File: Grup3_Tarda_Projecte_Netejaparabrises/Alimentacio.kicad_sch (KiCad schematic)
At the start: 8 parts, among them J1 Screw_Terminal_01x02, U1 LM1117MP-5.0

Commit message: canvis schematic 05-04-23
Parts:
- added D8: LED, symbol Device:LED
- added R6: 220, symbol Device:R
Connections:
- net +VCC: now also D8.2 (A)
- net GND: now also R6.2
- new net Vled: D8.1 (K), R6.1

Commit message: canvis schematic i README 07-04-2023
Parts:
- removed U1: LM1117MP-5.0, Package_TO_SOT_SMD:SOT-223-3_TabPin2, symbol Regulator_Linear:LM1117MP-5.0
- added IC1: L78S05CV, TO-220-STANDING, symbol L78S05CV:L78S05CV
- C2: value 1u -> 0.33u
- C4: value 1u -> 0.1u
- D2: value 15V -> 35V
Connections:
- net +VCC: now also IC1.3
- net GND: now also IC1.2
- net V_{in}: now also IC1.1
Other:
- moved on the sheet: C4
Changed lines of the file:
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@@
     (rev "v1.1.05042023")
   )
+  (junction (at 132.334 62.992) (diameter 0) (color 0 0 0 0)
+  )
   (junction (at 113.284 62.992) (diameter 0) (color 0 0 0 0)
   )
-  (junction (at 132.334 62.992) (diameter 0) (color 0 0 0 0)
-  )
   (junction (at 120.904 84.582) (diameter 0) (color 0 0 0 0)
   )
   (junction (at 132.334 84.582) (diameter 0) (color 0 0 0 0)
   )
+  (junction (at 157.988 62.992) (diameter 0) (color 0 0 0 0)
+  )
   (junction (at 178.054 62.992) (diameter 0) (color 0 0 0 0)
   )
@@
   (junction (at 147.574 84.582) (diameter 0) (color 0 0 0 0)
   )
-  (junction (at 157.988 62.992) (diameter 0) (color 0 0 0 0)
-  )
   (junction (at 157.988 84.582) (diameter 0) (color 0 0 0 0)
   )
@@
     (stroke (width 0) (type default))
   )
-  (wire (pts (xy 178.054 71.882) (xy 178.054 84.582))
-    (stroke (width 0) (type default))
-  )
-  (wire (pts (xy 178.054 62.992) (xy 178.054 64.262))
+  (wire (pts (xy 132.334 62.992) (xy 139.954 62.992))
+    (stroke (width 0) (type default))
+  )
+  (wire (pts (xy 178.054 72.136) (xy 178.054 84.582))
+    (stroke (width 0) (type default))
+  )
+  (wire (pts (xy 178.054 62.992) (xy 178.054 64.516))
     (stroke (width 0) (type default))
   )
@@
     (stroke (width 0) (type default))
   )
+  (wire (pts (xy 99.314 62.992) (xy 100.584 62.992))
+    (stroke (width 0) (type default))
+  )
+  (wire (pts (xy 178.054 62.992) (xy 181.864 62.992))
+    (stroke (width 0) (type default))
+  )
   (wire (pts (xy 155.194 62.992) (xy 157.988 62.992))
     (stroke (width 0) (type default))
   )
-  (wire (pts (xy 99.314 62.992) (xy 100.584 62.992))
-    (stroke (width 0) (type default))
-  )
-  (wire (pts (xy 178.054 62.992) (xy 181.864 62.992))
-    (stroke (width 0) (type default))
-  )
   (wire (pts (xy 120.904 62.992) (xy 120.904 64.262))
     (stroke (width 0) (type default))
@@
     (stroke (width 0) (type default))
   )
-  (wire (pts (xy 132.334 62.992) (xy 139.954 62.992))
-    (stroke (width 0) (type default))
-  )
   (wire (pts (xy 132.334 84.582) (xy 147.574 84.582))
     (stroke (width 0) (type default))
@@
     (stroke (width 0) (type default))
   )
-  (wire (pts (xy 167.894 69.342) (xy 167.894 84.582))
+  (wire (pts (xy 167.894 70.612) (xy 167.894 84.582))
     (stroke (width 0) (type default))
   )
@@
     (stroke (width 0) (type default))
   )
-  (wire (pts (xy 167.894 62.992) (xy 167.894 64.262))
+  (wire (pts (xy 167.894 62.992) (xy 167.894 65.532))
     (stroke (width 0) (type default))
   )
@@
     )
   )
-  (symbol (lib_id "Device:C_Polarized_Small_US") (at 167.894 66.802 0) (unit 1)
+  (symbol (lib_id "Device:C_Polarized_Small_US") (at 167.894 68.072 0) (unit 1)
     (in_bom yes) (on_board yes) (dnp no)
-    (property "Reference" "C4" (at 170.18 65.532 0)
-      (effects (font (size 1.27 1.27)) (justify left))
-    )
-    (property "Value" "1u" (at 170.18 68.072 0)
-      (effects (font (size 1.27 1.27)) (justify left))
-    )
-    (property "Footprint" "Capacitor_THT:C_Disc_D3.0mm_W1.6mm_P2.50mm" (at 167.894 66.802 0)
-      (effects (font (size 1.27 1.27)) hide)
-    )
-    (property "Datasheet" "~" (at 167.894 66.802 0)
+    (property "Reference" "C4" (at 170.18 66.802 0)
+      (effects (font (size 1.27 1.27)) (justify left))
+    )
+    (property "Value" "0.1u" (at 170.18 69.342 0)
+      (effects (font (size 1.27 1.27)) (justify left))
+    )
+    (property "Footprint" "Capacitor_THT:C_Disc_D3.0mm_W1.6mm_P2.50mm" (at 167.894 68.072 0)
+      (effects (font (size 1.27 1.27)) hide)
+    )
+    (property "Datasheet" "~" (at 167.894 68.072 0)
       (effects (font (size 1.27 1.27)) hide)
     )
@@
     )
   )
-  (symbol (lib_id "Regulator_Linear:LM1117MP-5.0") (at 147.574 62.992 0) (unit 1)
+  (symbol (lib_id "L78S05CV:L78S05CV") (at 147.574 62.992 0) (unit 1)
     (in_bom yes) (on_board yes) (dnp no) (fields_autoplaced)
-    (property "Reference" "U1" (at 147.574 56.896 0)
-      (effects (font (size 1.27 1.27)))
-    )
-    (property "Value" "LM1117MP-5.0" (at 147.574 59.436 0)
-      (effects (font (size 1.27 1.27)))
-    )
-    (property "Footprint" "Package_TO_SOT_SMD:SOT-223-3_TabPin2" (at 147.574 62.992 0)
-      (effects (font (size 1.27 1.27)) hide)
-    )
-    (property "Datasheet" "http://www.ti.com/lit/ds/symlink/lm1117.pdf" (at 147.574 62.992 0)
-      (effects (font (size 1.27 1.27)) hide)
+    (property "Reference" "IC1" (at 147.574 55.88 0)
+      (effects (font (size 1.27 1.27)))
+    )
+    (property "Value" "L78S05CV" (at 147.574 58.42 0)
+      (effects (font (size 1.27 1.27)))
+    )
+    (property "Footprint" "TO-220-STANDING" (at 147.574 62.992 0)
+      (effects (font (size 1.27 1.27)) (justify bottom) hide)
+    )
+    (property "Datasheet" "" (at 147.574 62.992 0)
+      (effects (font (size 1.27 1.27)) hide)
+    )
+    (property "VOUT" "5.0 V" (at 147.574 62.992 0)
+      (effects (font (size 1.27 1.27)) (justify bottom) hide)
+    )
+    (property "MANUFACTURER" "St Microelectronics" (at 147.574 62.992 0)
+      (effects (font (size 1.27 1.27)) (justify bottom) hide)
+    )
+    (property "CURRENT" "2.0 A" (at 147.574 62.992 0)
+      (effects (font (size 1.27 1.27)) (justify bottom) hide)
+    )
+    (property "TME" "L78S05CV" (at 147.574 62.992 0)
+      (effects (font (size 1.27 1.27)) (justify bottom) hide)
+    )
+    (property "PACKAGE" "TO-220" (at 147.574 62.992 0)
+      (effects (font (size 1.27 1.27)) (justify bottom) hide)
+    )
+    (property "VIN-MAX" "35.0 V" (at 147.574 62.992 0)
+      (effects (font (size 1.27 1.27)) (justify bottom) hide)
+    )
+    (property "VIN-MIN" "8.0 V" (at 147.574 62.992 0)
+      (effects (font (size 1.27 1.27)) (justify bottom) hide)
     )
     (pin "1")
@@
       (project "Grup3_Tarda_Projecte_Netejaparabrises"
         (path "/7ae78f34-680b-4fd9-8391-ce3e1c73c4b5/de573664-441d-44bf-8893-2d2e822d4a99"
-          (reference "U1") (unit 1)
+          (reference "IC1") (unit 1)
         )
       )
@@
       (effects (font (size 1.27 1.27)) (justify left))
     )
-    (property "Value" "1u" (at 134.366 69.596 0)
+    (property "Value" "0.33u" (at 134.366 69.596 0)
       (effects (font (size 1.27 1.27)) (justify left))
     )
@@
     )
   )
-  (symbol (lib_id "Device:C") (at 178.054 68.072 0) (unit 1)
+  (symbol (lib_id "Device:C") (at 178.054 68.326 0) (unit 1)
     (in_bom yes) (on_board yes) (dnp no)
-    (property "Reference" "C5" (at 181.102 66.802 0)
-      (effects (font (size 1.27 1.27)) (justify left))
-    )
-    (property "Value" "100n" (at 181.102 69.342 0)
-      (effects (font (size 1.27 1.27)) (justify left))
-    )
-    (property "Footprint" "Capacitor_SMD:C_0805_2012Metric" (at 179.0192 71.882 0)
-      (effects (font (size 1.27 1.27)) hide)
-    )
-    (property "Datasheet" "~" (at 178.054 68.072 0)
+    (property "Reference" "C5" (at 181.102 67.056 0)
+      (effects (font (size 1.27 1.27)) (justify left))
+    )
+    (property "Value" "100n" (at 181.102 69.596 0)
+      (effects (font (size 1.27 1.27)) (justify left))
+    )
+    (property "Footprint" "Capacitor_SMD:C_0805_2012Metric" (at 179.0192 72.136 0)
+      (effects (font (size 1.27 1.27)) hide)
+    )
+    (property "Datasheet" "~" (at 178.054 68.326 0)
       (effects (font (size 1.27 1.27)) hide)
     )
@@
       (effects (font (size 1.27 1.27)) (justify left))
     )
-    (property "Value" "15V" (at 107.95 69.596 90)
-      (effects (font (size 1.27 1.27)) (justify left))
-    )
+    (property "Value" "35V" (at 107.95 69.596 90)
+      (effects (font (size 1.27 1.27)) (justify left))
+    )

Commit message: canvis reles 07-04-2023
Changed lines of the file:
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@@
     (stroke (width 0) (type default))
   )
-  (polyline (pts (xy 60.96 44.958) (xy 60.706 96.774))
+  (polyline (pts (xy 60.96 44.958) (xy 60.96 96.266))
     (stroke (width 0) (type default))
   )
@@
     (stroke (width 0) (type default))
   )
-  (polyline (pts (xy 223.52 96.774) (xy 60.706 96.774))
+  (polyline (pts (xy 223.52 96.266) (xy 60.96 96.266))
     (stroke (width 0) (type default))
   )
@@
     (stroke (width 0) (type default))
   )
-  (polyline (pts (xy 223.52 44.958) (xy 223.52 96.774))
+  (polyline (pts (xy 223.52 44.958) (xy 223.52 96.266))
     (stroke (width 0) (type default))
   )

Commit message: GNDS 08042023
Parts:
- added FL1, FL2, FL3, FL4, FL5: BLM03HD331SZ1D, BEADC0603X33N, symbol BLM03HD331SZ1D:BLM03HD331SZ1D
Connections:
- net GND: now also FL1.2, FL2.2, FL3.2, FL4.2, FL5.1, FL5.2; no longer C1.2, C2.2, C4.2, C5.2, D2.2 (A), IC1.2, J1.2 (Pin_2), R6.2
- new net GNDPWR: C1.2, C2.2, C4.2, C5.2, D2.2 (A), FL1.1, FL2.1, FL3.1, FL4.1, IC1.2, J1.2 (Pin_2), R6.2
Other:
- note added: "GNDs"

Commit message: definitiuEsquematicsenseFootprints
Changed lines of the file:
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@@
       (effects (font (size 1.27 1.27)) hide)
     )
-    (property "Value" "GND2" (at 124.46 138.43 0)
+    (property "Value" "GND" (at 124.46 138.43 0)
       (effects (font (size 1.27 1.27)))
     )

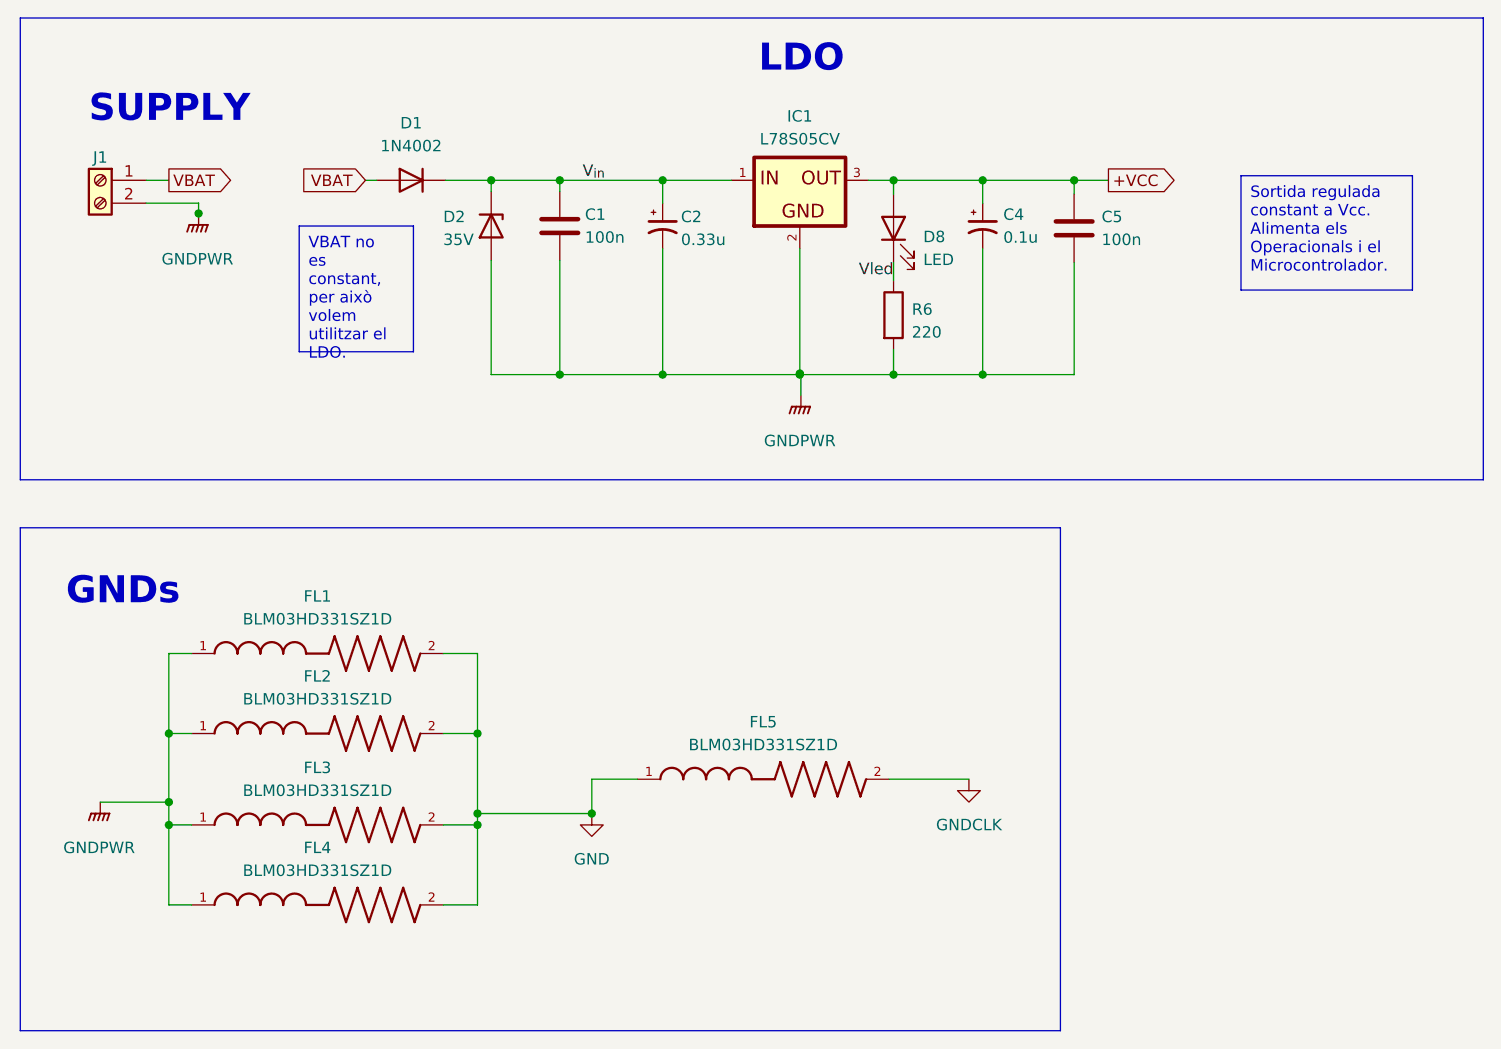
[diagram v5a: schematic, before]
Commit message: Modificacions finals assignacio footprints
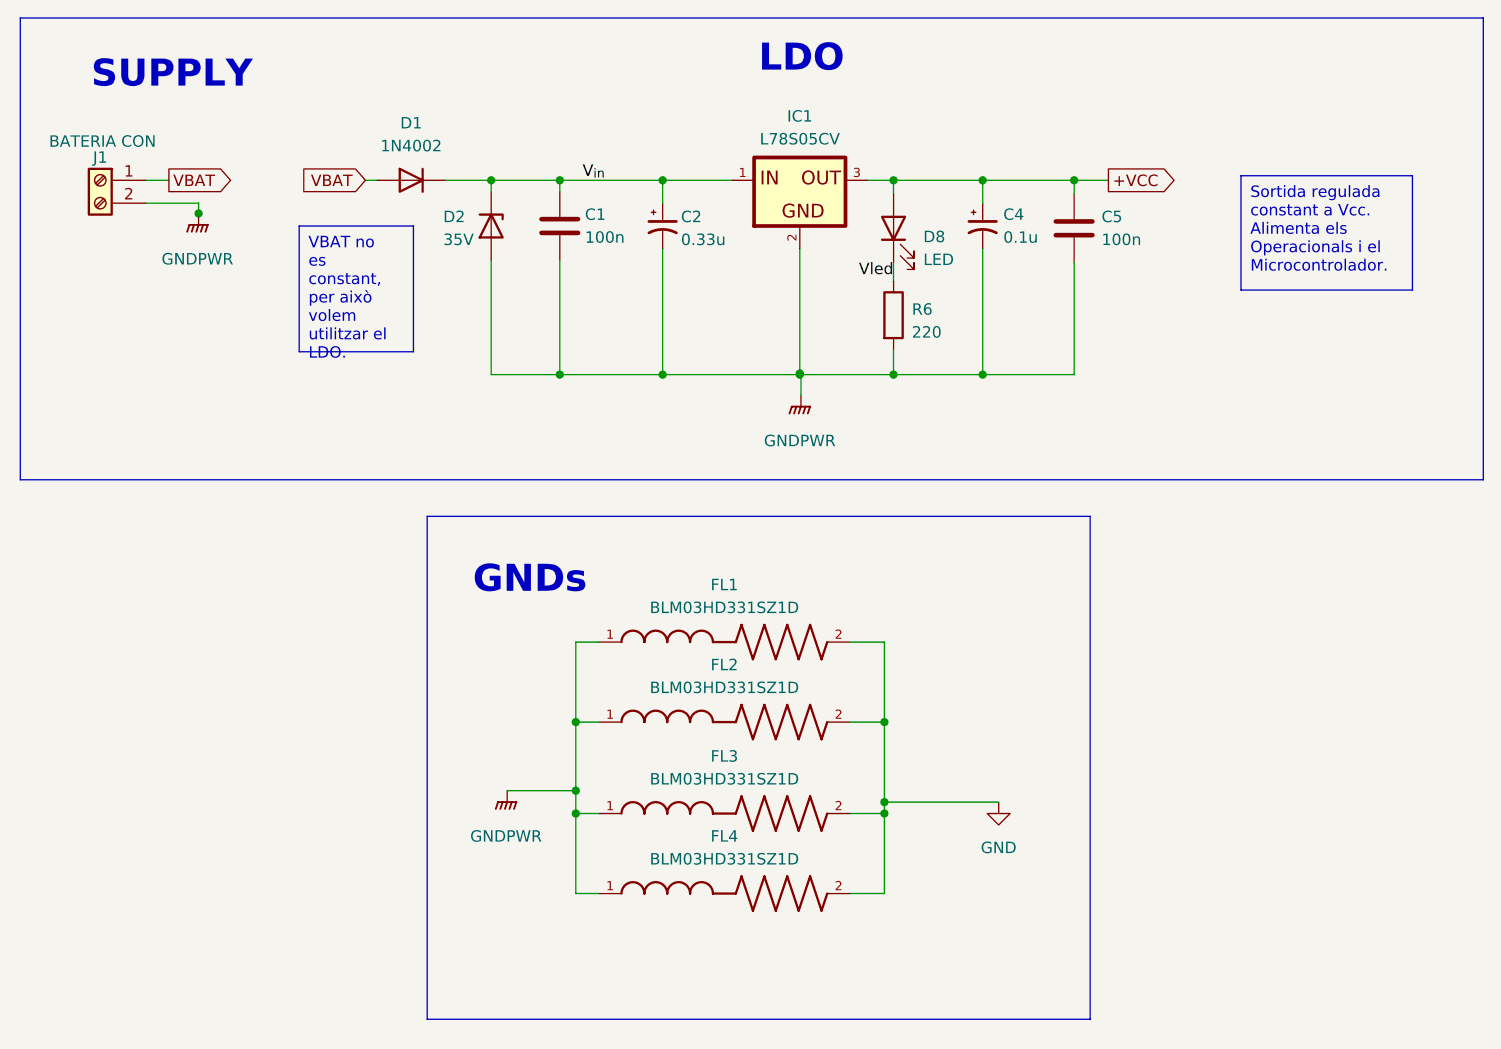
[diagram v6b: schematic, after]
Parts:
- removed FL5: BLM03HD331SZ1D, BEADC0603X33N, symbol BLM03HD331SZ1D:BLM03HD331SZ1D
- C1: footprint Capacitor_SMD:C_0805_2012Metric -> Capacitor_THT:C_Disc_D3.0mm_W1.6mm_P2.50mm
- D8: footprint (none) -> LED_SMD:LED_0805_2012Metric_Pad1.15x1.40mm_HandSolder
- FL1, FL2, FL3, FL4: footprint BEADC0603X33N -> BLM03HD331SZ1D:BEADC0603X33N
- IC1: footprint TO-220-STANDING -> L78S05CV:TO-220-STANDING
- J1: value Screw_Terminal_01x02 -> BATERIA CON
- R6: footprint (none) -> Resistor_SMD:R_0805_2012Metric_Pad1.20x1.40mm_HandSolder
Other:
- moved on the sheet: FL1, FL2, FL3, FL4
